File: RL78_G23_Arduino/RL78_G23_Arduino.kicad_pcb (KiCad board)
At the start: 2 copper layers, 100 x 57 mm, 37 parts, among them J1 Power, J2 Misc IOs, J3 Analog, J4 Misc IOs, J5 MiscIOs, J6 Communication, J7 Misc IOs, J8 MiscIOs, P1 USB_B, P2 POWER_JACKPTH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

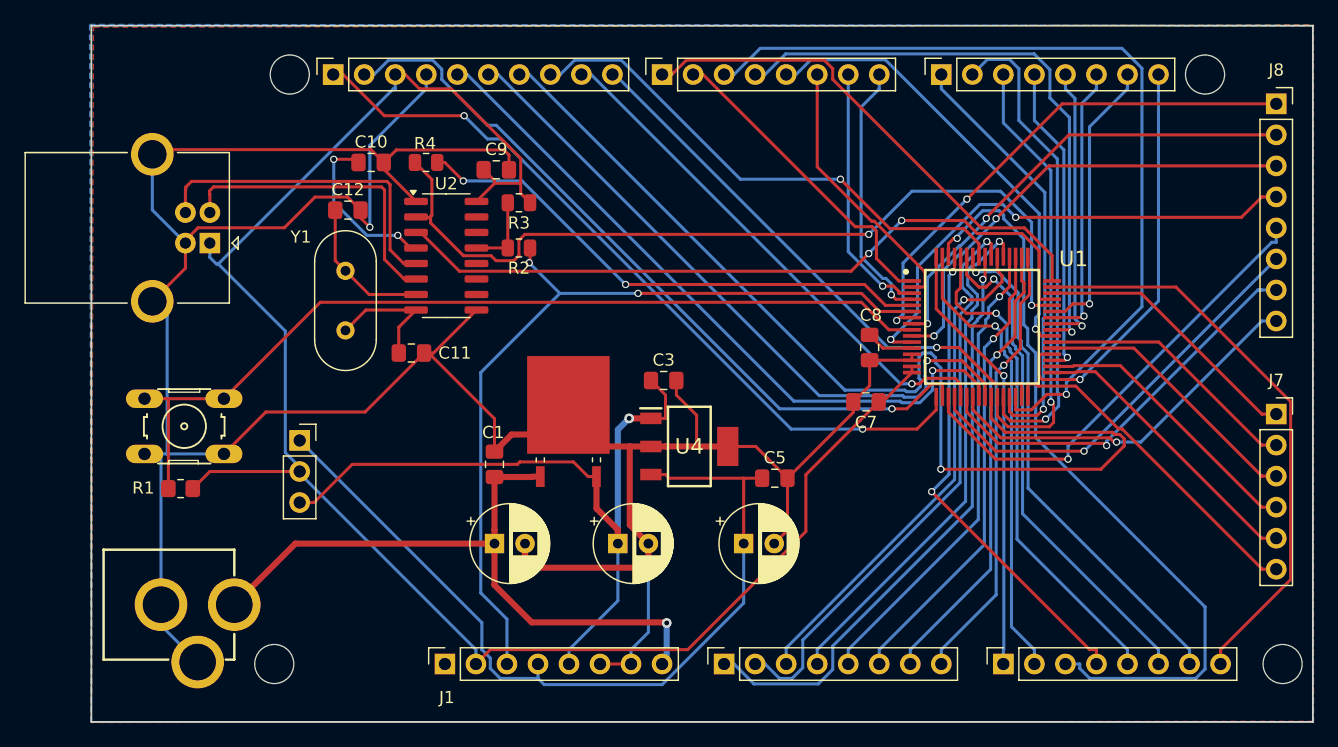
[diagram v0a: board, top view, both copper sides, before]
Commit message: Added a few other projects
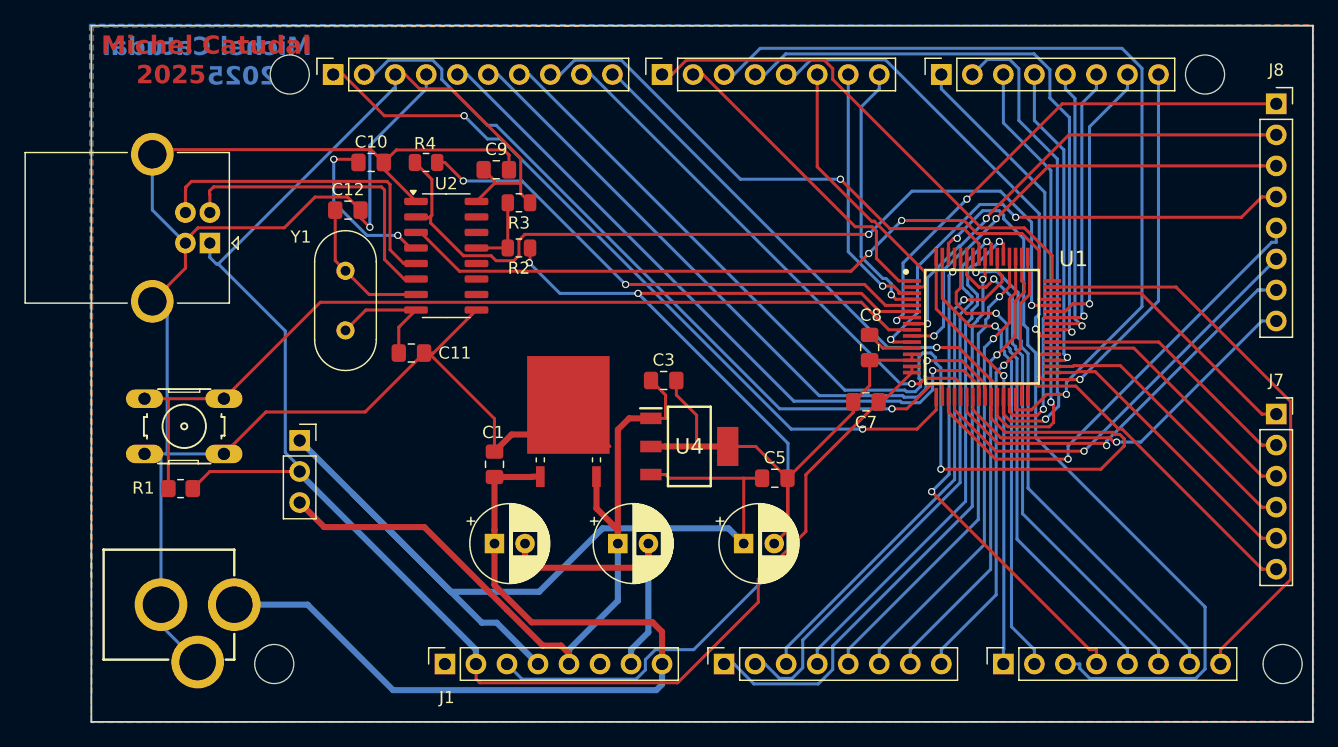
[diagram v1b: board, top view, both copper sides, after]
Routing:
- net /~{RESET}: track 68.1 -> 89.0 mm
- net /Vin: track 54.9 -> 70.9 mm, vias 1 -> 0
- net GND: track 247.8 -> 233.4 mm
- net +3.3V: track 69.8 -> 79.6 mm
- net VCC: track 146.1 -> 149.2 mm
- net +5V: track 61.1 -> 63.0 mm, vias 1 -> 0
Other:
- board text added: "Michel Catudal 2025"
